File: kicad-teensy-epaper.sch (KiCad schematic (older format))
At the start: 21 parts, among them J1 TEENSY3.2-72MHz, J2 HEADER-FEMALE-34POS-FFC-SMT-1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, Q1 Q_NMOS_GDS

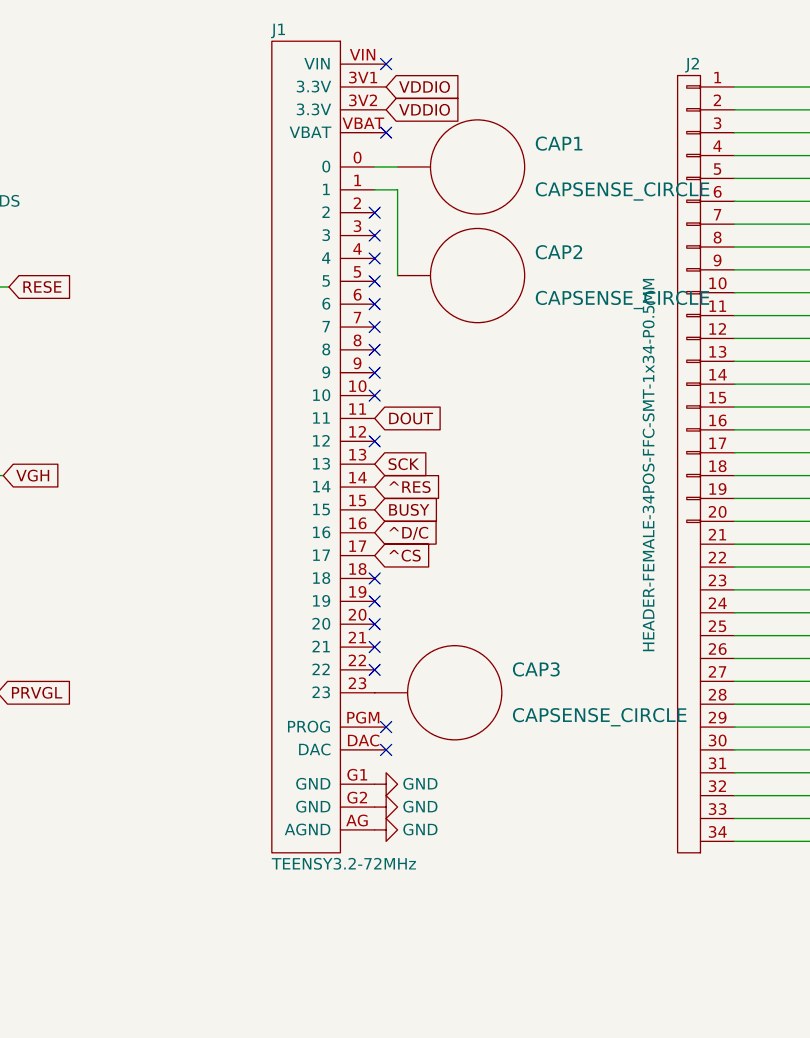
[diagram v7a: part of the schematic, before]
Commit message: Reworked layout for aesthetics
OSH Park order m5ay7bby on May 4th, 2017.
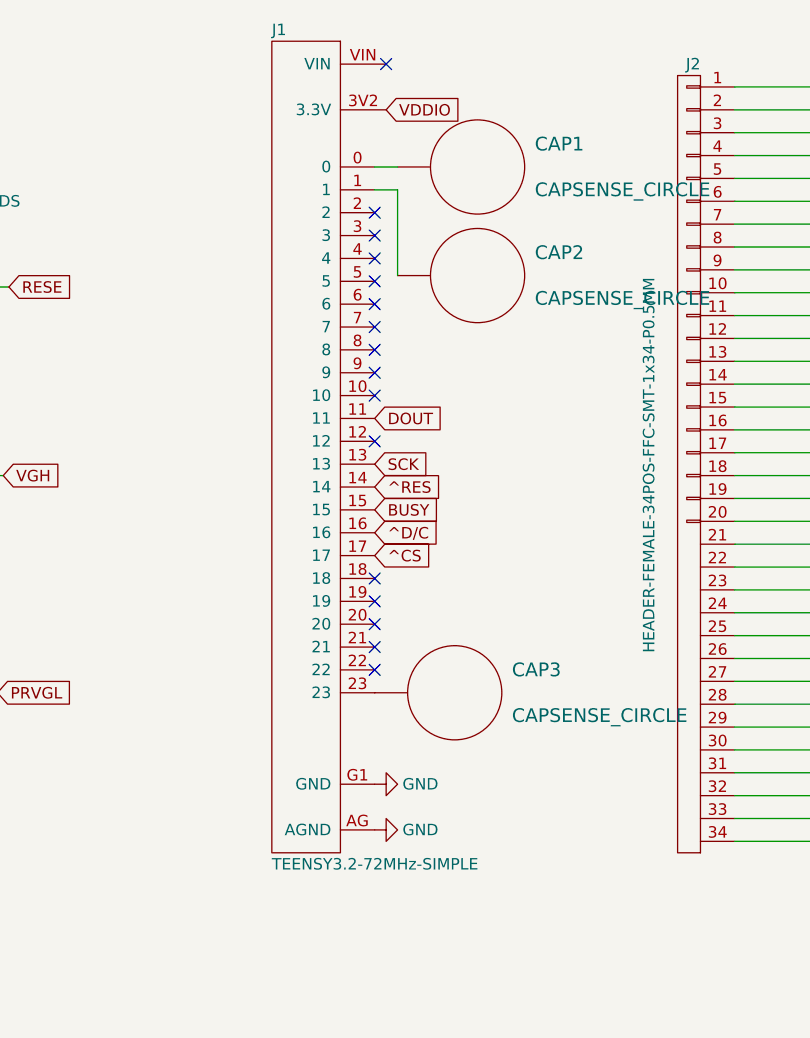
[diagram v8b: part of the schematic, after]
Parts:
- removed J1: TEENSY3.2-72MHz, Wickerlib:TEENSY-3.2-SILK, symbol TEENSY3.2-72MHz
- added J1: TEENSY3.2-72MHz-SIMPLE, Wickerlib:TEENSY-3.2-SILK-SIMPLE, symbol TEENSY3.2-72MHz-SIMPLE
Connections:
- net BUSY: now also J1.15
- net DOUT: now also J1.11
- net GND: now also J1.AG (AGND), J1.G1 (GND)
- net SCK: now also J1.13
- net VDDIO: now also J1.3V2 (3.3V)
- net ^CS: now also J1.17
- net ^D/C: now also J1.16
- net ^RES: now also J1.14
- net at CAP1.1 (BUTTON): now also J1.0
- net at CAP2.1 (BUTTON): now also J1.1
- net at CAP3.1 (BUTTON): now also J1.23
- no-connect marks 34 -> 31
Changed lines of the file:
@@
 VCOM
 $Comp
-L GND #PWR10
+L GND #PWR01
 U 1 1 5893E9A4
 P 8175 2775
-F 0 "#PWR10" H 8175 2525 50  0001 C CNN
+F 0 "#PWR01" H 8175 2525 50  0001 C CNN
 F 1 "GND" H 8175 2625 50  0000 C CNN
 F 2 "" H 8175 2775 50  0000 C CNN
@@
 Text GLabel 5050 3625 2    50   Input ~ 0
 ^CS
-Text GLabel 5100 1575 2    50   Input ~ 0
-VDDIO
 Text GLabel 5050 3225 2    50   Input ~ 0
 SCK
@@
 NoConn ~ 5050 3925
 NoConn ~ 5050 4025
-NoConn ~ 5100 4375
-NoConn ~ 5100 4475
 $Comp
 L CAP-CER-1UF-25V-X7R-0603 C2
@@
 $EndComp
 $Comp
-L GND #PWR12
+L GND #PWR02
 U 1 1 58941B65
 P 9400 1700
-F 0 "#PWR12" H 9400 1450 50  0001 C CNN
+F 0 "#PWR02" H 9400 1450 50  0001 C CNN
 F 1 "GND" H 9400 1550 50  0000 C CNN
 F 2 "" H 9400 1700 50  0000 C CNN
@@
 $EndComp
 $Comp
-L GND #PWR16
+L GND #PWR03
 U 1 1 58941CF9
 P 9400 3850
-F 0 "#PWR16" H 9400 3600 50  0001 C CNN
+F 0 "#PWR03" H 9400 3600 50  0001 C CNN
 F 1 "GND" H 9400 3700 50  0000 C CNN
 F 2 "" H 9400 3850 50  0000 C CNN
@@
 $EndComp
 $Comp
-L GND #PWR2
+L GND #PWR04
 U 1 1 58941E39
 P 2050 4550
-F 0 "#PWR2" H 2050 4300 50  0001 C CNN
+F 0 "#PWR04" H 2050 4300 50  0001 C CNN
 F 1 "GND" H 2050 4400 50  0000 C CNN
 F 2 "" H 2050 4550 50  0000 C CNN
@@
 $EndComp
 $Comp
-L GND #PWR1
+L GND #PWR05
 U 1 1 58941E7A
 P 1225 3850
-F 0 "#PWR1" H 1225 3600 50  0001 C CNN
+F 0 "#PWR05" H 1225 3600 50  0001 C CNN
 F 1 "GND" H 1225 3700 50  0000 C CNN
 F 2 "" H 1225 3850 50  0000 C CNN
@@
 $EndComp
 $Comp
-L GND #PWR5
+L GND #PWR06
 U 1 1 58941EFC
 P 2950 2950
-F 0 "#PWR5" H 2950 2700 50  0001 C CNN
+F 0 "#PWR06" H 2950 2700 50  0001 C CNN
 F 1 "GND" H 2950 2800 50  0000 C CNN
 F 2 "" H 2950 2950 50  0000 C CNN
@@
 Connection ~ 1225 3275
 $Comp
-L GND #PWR13
+L GND #PWR07
 U 1 1 58952731
 P 9400 2150
-F 0 "#PWR13" H 9400 1900 50  0001 C CNN
+F 0 "#PWR07" H 9400 1900 50  0001 C CNN
 F 1 "GND" H 9400 2000 50  0000 C CNN
 F 2 "" H 9400 2150 50  0000 C CNN
@@
 $EndComp
 $Comp
-L GND #PWR6
+L GND #PWR08
 U 1 1 58953BD1
 P 5050 4625
-F 0 "#PWR6" H 5050 4375 50  0001 C CNN
+F 0 "#PWR08" H 5050 4375 50  0001 C CNN
 F 1 "GND" V 5050 4425 50  0000 C CNN
 F 2 "" H 5050 4625 50  0000 C CNN
@@
 $EndComp
 $Comp
-L GND #PWR15
+L GND #PWR09
 U 1 1 58953E27
 P 9400 2975
-F 0 "#PWR15" H 9400 2725 50  0001 C CNN
+F 0 "#PWR09" H 9400 2725 50  0001 C CNN
 F 1 "GND" H 9400 2825 50  0000 C CNN
 F 2 "" H 9400 2975 50  0000 C CNN
@@
 $EndComp
 $Comp
-L GND #PWR4
+L GND #PWR010
 U 1 1 58954CBF
 P 2900 4625
-F 0 "#PWR4" H 2900 4375 50  0001 C CNN
+F 0 "#PWR010" H 2900 4375 50  0001 C CNN
 F 1 "GND" H 2900 4475 50  0000 C CNN
 F 2 "" H 2900 4625 50  0000 C CNN
@@
 $EndComp
 $Comp
-L GND #PWR14
+L GND #PWR011
 U 1 1 58954E61
 P 9400 2575
-F 0 "#PWR14" H 9400 2325 50  0001 C CNN
+F 0 "#PWR011" H 9400 2325 50  0001 C CNN
 F 1 "GND" V 9400 2375 50  0000 C CNN
 F 2 "" H 9400 2575 50  0000 C CNN
@@
 $EndComp
 $Comp
-L GND #PWR3
+L GND #PWR012
 U 1 1 58955108
 P 2900 3850
-F 0 "#PWR3" H 2900 3600 50  0001 C CNN
+F 0 "#PWR012" H 2900 3600 50  0001 C CNN
 F 1 "GND" V 2900 3650 50  0000 C CNN
 F 2 "" H 2900 3850 50  0000 C CNN
@@
 VSL
 $Comp
-L GND #PWR11
+L GND #PWR013
 U 1 1 589557C5
 P 9375 3350
-F 0 "#PWR11" H 9375 3100 50  0001 C CNN
+F 0 "#PWR013" H 9375 3100 50  0001 C CNN
 F 1 "GND" V 9375 3150 50  0000 C CNN
 F 2 "" H 9375 3350 50  0000 C CNN
@@
 $EndComp
 $Comp
-L GND #PWR8
+L GND #PWR014
 U 1 1 58956AE7
 P 5050 4825
-F 0 "#PWR8" H 5050 4575 50  0001 C CNN
+F 0 "#PWR014" H 5050 4575 50  0001 C CNN
 F 1 "GND" V 5050 4625 50  0000 C CNN
 F 2 "" H 5050 4825 50  0000 C CNN
@@
 	0    -1   -1   0
 $EndComp
-$Comp
-L GND #PWR7
-U 1 1 58956B28
-P 5050 4725
-F 0 "#PWR7" H 5050 4475 50  0001 C CNN
-F 1 "GND" V 5050 4525 50  0000 C CNN
-F 2 "" H 5050 4725 50  0000 C CNN
-F 3 "" H 5050 4725 50  0000 C CNN
-	1    5050 4725
-	0    -1   -1   0
-$EndComp
-$Comp
-L TEENSY3.2-72MHz J1
-U 1 1 58956D44
-P 4800 3175
-F 0 "J1" H 4600 5025 50  0000 L CNN
-F 1 "TEENSY3.2-72MHz" H 4600 1375 50  0000 L CNN
-F 2 "Wickerlib:TEENSY-3.2-SILK" V 4550 4325 50  0001 C CIN
-F 3 "https://www.pjrc.com/teensy/" H 5050 3825 5   0001 C CNN
-F 4 "TEENSY 3.2 32BIT 72MHZ" V 4550 4325 50  0001 C CIN "Description"
-F 5 "PJRC" V 4550 4325 50  0001 C CIN "MF_Name"
-F 6 "TEENSY3.2" V 4550 4325 50  0001 C CIN "MF_PN"
-F 7 "PJRC" V 4550 4325 50  0001 C CIN "S1_Name"
-F 8 "TEENSY3.2" V 4550 4325 50  0001 C CIN "S1_PN"
-	1    4800 3175
-	1    0    0    -1
-$EndComp
 NoConn ~ 5100 1475
-NoConn ~ 5100 1775
 Wire Wire Line
 	2550 2125 2650 2125
@@
 NoConn ~ 7775 4875
 $Comp
-L GND #PWR9
+L GND #PWR015
 U 1 1 58DB75A7
 P 8150 3675
-F 0 "#PWR9" H 8150 3425 50  0001 C CNN
+F 0 "#PWR015" H 8150 3425 50  0001 C CNN
 F 1 "GND" H 8150 3525 50  0000 C CNN
 F 2 "" H 8150 3675 50  0000 C CNN
@@
 	1    0    0    -1
 $EndComp
+$Comp
+L TEENSY3.2-72MHz-SIMPLE J1
+U 1 1 590B75A7
+P 4800 3175
+F 0 "J1" H 4600 5025 50  0000 L CNN
+F 1 "TEENSY3.2-72MHz-SIMPLE" H 4600 1375 50  0000 L CNN
+F 2 "Wickerlib:TEENSY-3.2-SILK-SIMPLE" V 4550 4325 50  0001 C CIN
+F 3 "https://www.pjrc.com/teensy/" H 5050 3825 5   0001 C CNN
+F 4 "TEENSY 3.2 32BIT 72MHZ" V 4550 4325 50  0001 C CIN "Description"
+F 5 "PJRC" V 4550 4325 50  0001 C CIN "MF_Name"
+F 6 "TEENSY3.2" V 4550 4325 50  0001 C CIN "MF_PN"
+F 7 "PJRC" V 4550 4325 50  0001 C CIN "S1_Name"
+F 8 "TEENSY3.2" V 4550 4325 50  0001 C CIN "S1_PN"
+	1    4800 3175
+	1    0    0    -1
+$EndComp
